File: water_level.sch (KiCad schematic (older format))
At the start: 14 parts, among them U2 LTV-847

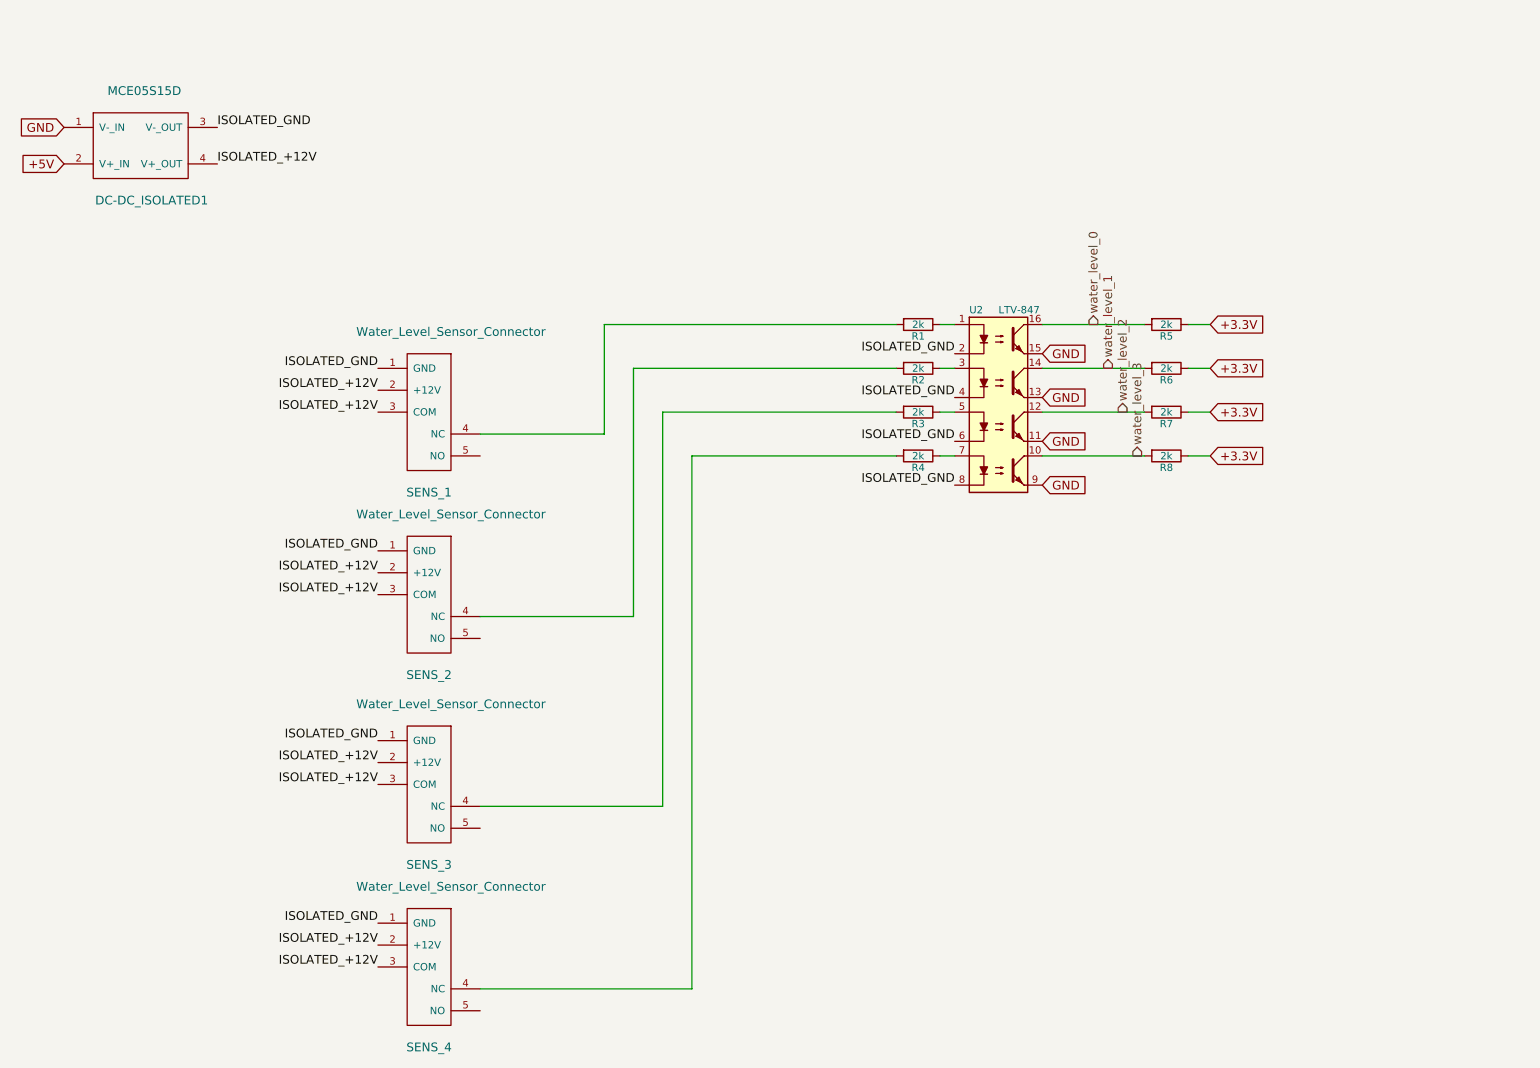
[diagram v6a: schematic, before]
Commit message: before new pcb; - the order of the gpio pins have changed in accordance with olinuxino - indicator leds have been added for debugging - ad current pin added for debugging
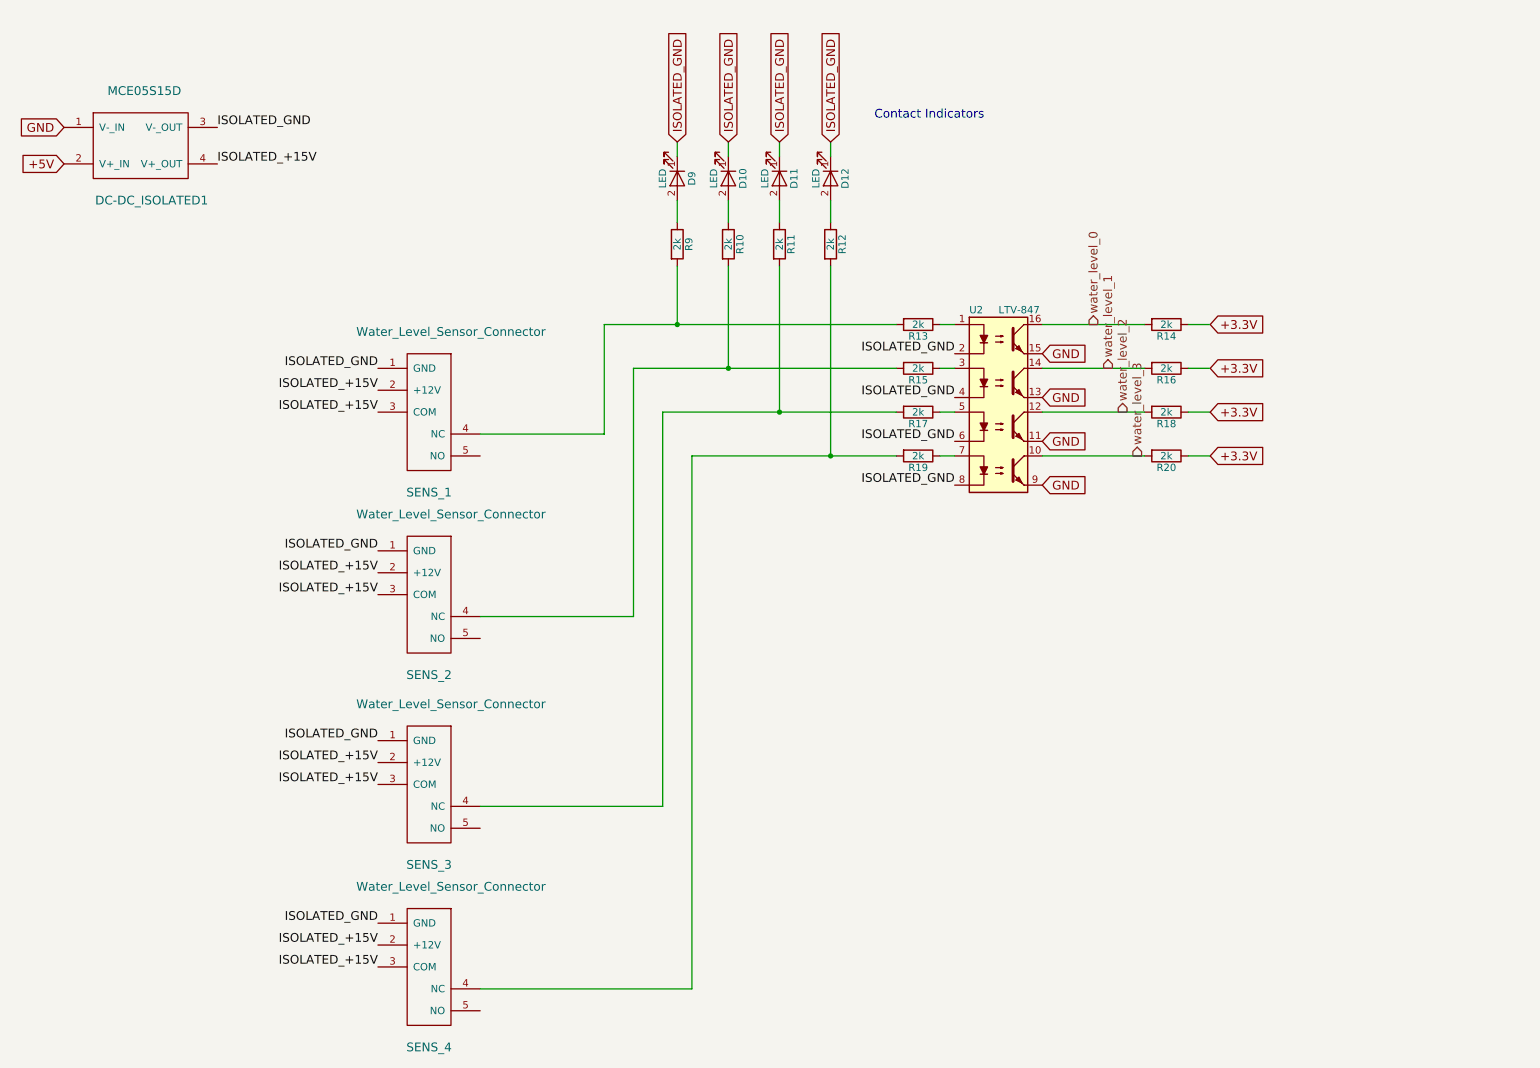
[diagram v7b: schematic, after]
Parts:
- added D10, D11, D12, D9: LED, LEDs:LED_1206, symbol LED
- added R10, R11, R12, R9: 2k, Resistors_SMD:R_1206_HandSoldering, symbol R
- renumbered R1 to R13, R5 to R14, R2 to R15, R6 to R16, R3 to R17, R7 to R18, R4 to R19, R8 to R20
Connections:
- net ISOLATED_GND: now also D10.1 (K), D11.1 (K), D12.1 (K), D9.1 (K)
- net at R13.2, SENS_1.4 (NC): now also R9.2
- net at R15.2, SENS_2.4 (NC): now also R10.2
- net at R17.2, SENS_3.4 (NC): now also R11.2
- net at R19.2, SENS_4.4 (NC): now also R12.2
- net ISOLATED_+12V renamed ISOLATED_+15V
- new net: D11.2 (A), R11.1
- new net: D12.2 (A), R12.1
- new net: D10.2 (A), R10.1
- new net: D9.2 (A), R9.1
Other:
- note added: "Contact Indicators"
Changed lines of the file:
@@
 $EndComp
 $Comp
-L R R1
+L R R13
 U 1 1 56150D2B
 P 6800 2550
-F 0 "R1" V 6880 2550 50  0000 C CNN
+F 0 "R13" V 6880 2550 50  0000 C CNN
 F 1 "2k" V 6800 2550 50  0000 C CNN
 F 2 "Resistors_SMD:R_1206_HandSoldering" V 6730 2550 30  0001 C CNN
@@
 $EndComp
 $Comp
-L R R2
+L R R15
 U 1 1 56150E0B
 P 6800 2850
-F 0 "R2" V 6880 2850 50  0000 C CNN
+F 0 "R15" V 6880 2850 50  0000 C CNN
 F 1 "2k" V 6800 2850 50  0000 C CNN
 F 2 "Resistors_SMD:R_1206_HandSoldering" V 6730 2850 30  0001 C CNN
-F 3 "" H 6800 2850 30  0000 C CNN
+F 3 "http://hu.farnell.com/multicomp/mcwr12x2001ftl/res-thick-film-2k-1-0-25w-1206/dp/2447495" H 6800 2850 30  0001 C CNN
 	1    6800 2850
 	0    1    1    0
 $EndComp
 $Comp
-L R R3
+L R R17
 U 1 1 56150E41
 P 6800 3150
-F 0 "R3" V 6880 3150 50  0000 C CNN
+F 0 "R17" V 6880 3150 50  0000 C CNN
 F 1 "2k" V 6800 3150 50  0000 C CNN
 F 2 "Resistors_SMD:R_1206_HandSoldering" V 6730 3150 30  0001 C CNN
-F 3 "" H 6800 3150 30  0000 C CNN
+F 3 "http://hu.farnell.com/multicomp/mcwr12x2001ftl/res-thick-film-2k-1-0-25w-1206/dp/2447495" H 6800 3150 30  0001 C CNN
 	1    6800 3150
 	0    1    1    0
 $EndComp
 $Comp
-L R R4
+L R R19
 U 1 1 56150E74
 P 6800 3450
-F 0 "R4" V 6880 3450 50  0000 C CNN
+F 0 "R19" V 6880 3450 50  0000 C CNN
 F 1 "2k" V 6800 3450 50  0000 C CNN
 F 2 "Resistors_SMD:R_1206_HandSoldering" V 6730 3450 30  0001 C CNN
-F 3 "" H 6800 3450 30  0000 C CNN
+F 3 "http://hu.farnell.com/multicomp/mcwr12x2001ftl/res-thick-film-2k-1-0-25w-1206/dp/2447495" H 6800 3450 30  0001 C CNN
 	1    6800 3450
 	0    1    1    0
 $EndComp
 $Comp
-L R R5
+L R R14
 U 1 1 56154BC4
 P 8500 2550
-F 0 "R5" V 8580 2550 50  0000 C CNN
+F 0 "R14" V 8580 2550 50  0000 C CNN
 F 1 "2k" V 8500 2550 50  0000 C CNN
 F 2 "Resistors_SMD:R_1206_HandSoldering" V 8430 2550 30  0001 C CNN
-F 3 "" H 8500 2550 30  0000 C CNN
+F 3 "http://hu.farnell.com/multicomp/mcwr12x2001ftl/res-thick-film-2k-1-0-25w-1206/dp/2447495" H 8500 2550 30  0001 C CNN
 	1    8500 2550
 	0    1    1    0
 $EndComp
 $Comp
-L R R6
+L R R16
 U 1 1 56154C43
 P 8500 2850
-F 0 "R6" V 8580 2850 50  0000 C CNN
+F 0 "R16" V 8580 2850 50  0000 C CNN
 F 1 "2k" V 8500 2850 50  0000 C CNN
 F 2 "Resistors_SMD:R_1206_HandSoldering" V 8430 2850 30  0001 C CNN
-F 3 "" H 8500 2850 30  0000 C CNN
+F 3 "http://hu.farnell.com/multicomp/mcwr12x2001ftl/res-thick-film-2k-1-0-25w-1206/dp/2447495" H 8500 2850 30  0001 C CNN
 	1    8500 2850
 	0    1    1    0
 $EndComp
 $Comp
-L R R7
+L R R18
 U 1 1 56154CA7
 P 8500 3150
-F 0 "R7" V 8580 3150 50  0000 C CNN
+F 0 "R18" V 8580 3150 50  0000 C CNN
 F 1 "2k" V 8500 3150 50  0000 C CNN
 F 2 "Resistors_SMD:R_1206_HandSoldering" V 8430 3150 30  0001 C CNN
-F 3 "" H 8500 3150 30  0000 C CNN
+F 3 "http://hu.farnell.com/multicomp/mcwr12x2001ftl/res-thick-film-2k-1-0-25w-1206/dp/2447495" H 8500 3150 30  0001 C CNN
 	1    8500 3150
 	0    1    1    0
 $EndComp
 $Comp
-L R R8
+L R R20
 U 1 1 56154CFE
 P 8500 3450
-F 0 "R8" V 8580 3450 50  0000 C CNN
+F 0 "R20" V 8580 3450 50  0000 C CNN
 F 1 "2k" V 8500 3450 50  0000 C CNN
 F 2 "Resistors_SMD:R_1206_HandSoldering" V 8430 3450 30  0001 C CNN
-F 3 "" H 8500 3450 30  0000 C CNN
+F 3 "http://hu.farnell.com/multicomp/mcwr12x2001ftl/res-thick-film-2k-1-0-25w-1206/dp/2447495" H 8500 3450 30  0001 C CNN
 	1    8500 3450
 	0    1    1    0
@@
 ISOLATED_GND
 Text Label 2000 1450 0    60   ~ 0
-ISOLATED_+12V
+ISOLATED_+15V
 Text Label 3100 3000 2    60   ~ 0
-ISOLATED_+12V
+ISOLATED_+15V
 Text Label 3100 4250 2    60   ~ 0
-ISOLATED_+12V
+ISOLATED_+15V
 Text Label 3100 5550 2    60   ~ 0
-ISOLATED_+12V
+ISOLATED_+15V
 Text Label 3100 6800 2    60   ~ 0
-ISOLATED_+12V
+ISOLATED_+15V
 Text Label 3100 3150 2    60   ~ 0
-ISOLATED_+12V
+ISOLATED_+15V
 Text Label 3100 4400 2    60   ~ 0
-ISOLATED_+12V
+ISOLATED_+15V
 Text Label 3100 5700 2    60   ~ 0
-ISOLATED_+12V
+ISOLATED_+15V
 Text Label 3100 6950 2    60   ~ 0
-ISOLATED_+12V
+ISOLATED_+15V
 Wire Wire Line
 	3800 3300 4650 3300
@@
 	1    0    0    -1
 $EndComp
+$Comp
+L R R11
+U 1 1 59403F80
+P 5850 2000
+F 0 "R11" V 5930 2000 50  0000 C CNN
+F 1 "2k" V 5850 2000 50  0000 C CNN
+F 2 "Resistors_SMD:R_1206_HandSoldering" V 5780 2000 50  0001 C CNN
+F 3 "http://hu.farnell.com/multicomp/mcwr12x2001ftl/res-thick-film-2k-1-0-25w-1206/dp/2447495" H 5850 2000 50  0001 C CNN
+	1    5850 2000
+	1    0    0    -1
+$EndComp
+$Comp
+L LED D11
+U 1 1 59403F87
+P 5850 1550
+F 0 "D11" H 5850 1650 50  0000 C CNN
+F 1 "LED" H 5850 1450 50  0000 C CNN
+F 2 "LEDs:LED_1206" H 5850 1550 50  0001 C CNN
+F 3 "http://hu.farnell.com/lumex/sml-lx15syc-tr/led-yellow-3mm-60mcd-590nm/dp/2062220" H 5850 1550 50  0001 C CNN
+	1    5850 1550
+	0    1    1    0
+$EndComp
+Text GLabel 5850 1300 1    60   Input ~ 0
+ISOLATED_GND
+Wire Wire Line
+	5850 1300 5850 1400
+Wire Wire Line
+	5850 1700 5850 1850
+Wire Wire Line
+	5850 2150 5850 3150
+$Comp
+L R R12
+U 1 1 59405398
+P 6200 2000
+F 0 "R12" V 6280 2000 50  0000 C CNN
+F 1 "2k" V 6200 2000 50  0000 C CNN
+F 2 "Resistors_SMD:R_1206_HandSoldering" V 6130 2000 50  0001 C CNN
+F 3 "http://hu.farnell.com/multicomp/mcwr12x2001ftl/res-thick-film-2k-1-0-25w-1206/dp/2447495" H 6200 2000 50  0001 C CNN
+	1    6200 2000
+	1    0    0    -1
+$EndComp
+$Comp
+L LED D12
+U 1 1 5940539F
+P 6200 1550
+F 0 "D12" H 6200 1650 50  0000 C CNN
+F 1 "LED" H 6200 1450 50  0000 C CNN
+F 2 "LEDs:LED_1206" H 6200 1550 50  0001 C CNN
+F 3 "http://hu.farnell.com/lumex/sml-lx15syc-tr/led-yellow-3mm-60mcd-590nm/dp/2062220" H 6200 1550 50  0001 C CNN
+	1    6200 1550
+	0    1    1    0
+$EndComp
+Text GLabel 6200 1300 1    60   Input ~ 0
+ISOLATED_GND
+Wire Wire Line
+	6200 1300 6200 1400
+Wire Wire Line
+	6200 1700 6200 1850
+$Comp
+L R R10
+U 1 1 5940552E
+P 5500 2000
+F 0 "R10" V 5580 2000 50  0000 C CNN
+F 1 "2k" V 5500 2000 50  0000 C CNN
+F 2 "Resistors_SMD:R_1206_HandSoldering" V 5430 2000 50  0001 C CNN
+F 3 "http://hu.farnell.com/multicomp/mcwr12x2001ftl/res-thick-film-2k-1-0-25w-1206/dp/2447495" H 5500 2000 50  0001 C CNN
+	1    5500 2000
+	1    0    0    -1
+$EndComp
+$Comp
+L LED D10
+U 1 1 59405535
+P 5500 1550
+F 0 "D10" H 5500 1650 50  0000 C CNN
+F 1 "LED" H 5500 1450 50  0000 C CNN
+F 2 "LEDs:LED_1206" H 5500 1550 50  0001 C CNN
+F 3 "http://hu.farnell.com/lumex/sml-lx15syc-tr/led-yellow-3mm-60mcd-590nm/dp/2062220" H 5500 1550 50  0001 C CNN
+	1    5500 1550
+	0    1    1    0
+$EndComp
+Text GLabel 5500 1300 1    60   Input ~ 0
+ISOLATED_GND
+Wire Wire Line
+	5500 1300 5500 1400
+Wire Wire Line
+	5500 1700 5500 1850
+Wire Wire Line
+	5500 2150 5500 2850
+$Comp
+L R R9
+U 1 1 5940560C
+P 5150 2000
+F 0 "R9" V 5230 2000 50  0000 C CNN
+F 1 "2k" V 5150 2000 50  0000 C CNN
+F 2 "Resistors_SMD:R_1206_HandSoldering" V 5080 2000 50  0001 C CNN
+F 3 "http://hu.farnell.com/multicomp/mcwr12x2001ftl/res-thick-film-2k-1-0-25w-1206/dp/2447495" H 5150 2000 50  0001 C CNN
+	1    5150 2000
+	1    0    0    -1
+$EndComp
+$Comp
+L LED D9
+U 1 1 59405613
+P 5150 1550
+F 0 "D9" H 5150 1650 50  0000 C CNN
+F 1 "LED" H 5150 1450 50  0000 C CNN
+F 2 "LEDs:LED_1206" H 5150 1550 50  0001 C CNN
+F 3 "http://hu.farnell.com/lumex/sml-lx15syc-tr/led-yellow-3mm-60mcd-590nm/dp/2062220" H 5150 1550 50  0001 C CNN
+	1    5150 1550
+	0    1    1    0
+$EndComp
+Text GLabel 5150 1300 1    60   Input ~ 0
+ISOLATED_GND
+Wire Wire Line
+	5150 1300 5150 1400
+Wire Wire Line
+	5150 1700 5150 1850
+Text Notes 6500 1150 0    60   ~ 0
+Contact Indicators
+Wire Wire Line
+	5150 2150 5150 2550
+Connection ~ 5150 2550
+Connection ~ 5500 2850
+Connection ~ 5850 3150
+Wire Wire Line
+	6200 2150 6200 3450
+Connection ~ 6200 3450
 $EndSCHEMATC

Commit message: changes towards the liteSOM drive.
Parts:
- DC-DC_ISOLATED1: 3W (none) -> http://hu.farnell.com/xp-power/jce0324s15/dc-dc-converter-1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
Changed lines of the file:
@@
 LIBS:vtx-214-015-112
 LIBS:viztisztito-cache
+LIBS:dc-dc
+LIBS:cmos_ieee
+LIBS:zetex
+LIBS:RFSolutions
 EELAYER 25 0
 EELAYER END
 $Descr A4 11693 8268
 encoding utf-8
-Sheet 3 5
+Sheet 3 6
 Title ""
 Date ""
@@
 F 2 "water:MCE05S15D" H 1500 950 60  0001 C CNN
 F 3 "http://hu.farnell.com/multicomp/mce05s15d/dc-dc-converter-1w-single-o-p/dp/2079693" H 1500 950 60  0001 C CNN
+F 4 "http://hu.farnell.com/xp-power/jce0324s15/dc-dc-converter-15v-0-2a-dip/dp/2475933" H 1500 950 60  0001 C CNN "3W"
 	1    1500 950
 	1    0    0    -1
